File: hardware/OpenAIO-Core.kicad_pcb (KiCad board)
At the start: 6 copper layers, 23 x 20.1 mm, 91 parts, among them J23 SCL, J26 SDA, J30 5V, J34 GND, J35 GND, J37 5V, J38 CAM, J39 VTX, J40 GND, J42 4V5, J43 GND, J44 PIO_TX0, J45 PIO_RX0, J48 RX0, J49 TX0, J50 GND, J52 4V5, J53 GND, J54 TX1, J55 RX1, J91 Core_LGA, Q1 AP1606, Q2 AP1606, U1 TS2306A 240GF MSM 9_C2976675, U10 COS8051SOT, U11 TLV7031DPWR, U2 RP2354A, U6 LP5912-1.8DRVR, U7 LP5912-3.3DRVR, U8 BMI270, U9 SN74LVC1G3157DTBR, X1 XTM25012000JT00351001

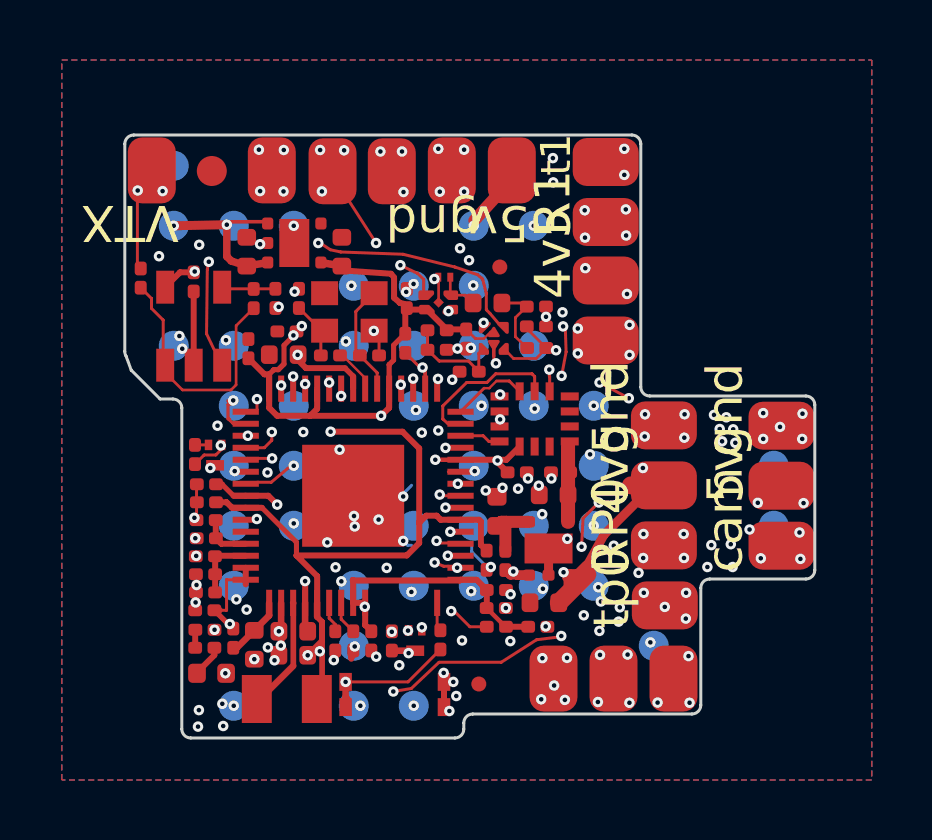
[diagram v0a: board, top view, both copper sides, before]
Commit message: DFM: solder mask 0.04 mm / 0.09 mm web, named X2SON gangs, L3-U25 gap (DFM-12, DFM-11)
Board setup on both boards: solder mask expansion 0 -> 0.04 mm (NextPCB
minimum opening), minimum mask web 0.09 mm (NextPCB green dam; the Core had
none). That made KiCad report 9 Core and 9 Base mask bridges.

Named exceptions, only where the datasheet land pattern has pad gaps below
2 x 0.04 + 0.09 = 0.17 mm: "Mask gang: U9 X2SON-6", "Mask gang: U11
X2SON-4" (Core) and "Mask gang: U23 X2SON-4" (Base), bridged_mask with
severity ignore. KiCad 10.0.6 only matches bridged_mask on item A (an
A && B condition never fires), so each rule names its footprint; no bridge
leaves those footprints.

Real bridges fixed by moving parts (track ends and vias in the pads dragged
along, Base, unconnected 0):
- R65/R66/R64 0201 row +0.02/+0.04/+0.06 mm x (gaps 0.155 -> 0.175)
- R83 -0.015 mm y (R57-R83 gap 0.165 -> 0.18)
- FID1/FID2 (B) 0.04 mm away from U24.11 (web 0.067 -> 0.107)
- U25 -0.015 mm x with its +3V3 via (U25.3-C19.1 0.155 -> 0.17)

DFM-11: U25 (INA186, SC70) and its cap C104 move -0.14 mm y; the L3-U25
body gap goes from 0.075 to 0.215 mm. The CURR track end at U25.6 was set
to (66.00, 52.18) to keep 0.14 mm from the +BATT via at (65.46, 51.83).

With the Core web on, KiCad also reports 5 pad labels clipped by the mask
(single-item). Four of them moved 0.2-0.3 mm (gnd x3, tp0); that also
cleared some old label overlaps. R1 (118.07, 46.86) stays for the owner's
silk pass. The Base '+' label moved 0.1 mm off C104.

DRC (refill, parity) against f193d5f: Core silk_over_copper 12 -> 12, Base
silk_over_copper 27 -> 20, no solder_mask_bridge, every other count
unchanged, unconnected 0 on both boards. DC solve: +BATT 0.582 -> 0.584,
GND 0.358 -> 0.358 mOhm.

Co-Authored-By: Claude Opus 5.5 <noreply@anthropic.com>
Claude-Session: https://claude.ai/code/session_01KTp3FLjVXfXdWrkmr6af7d
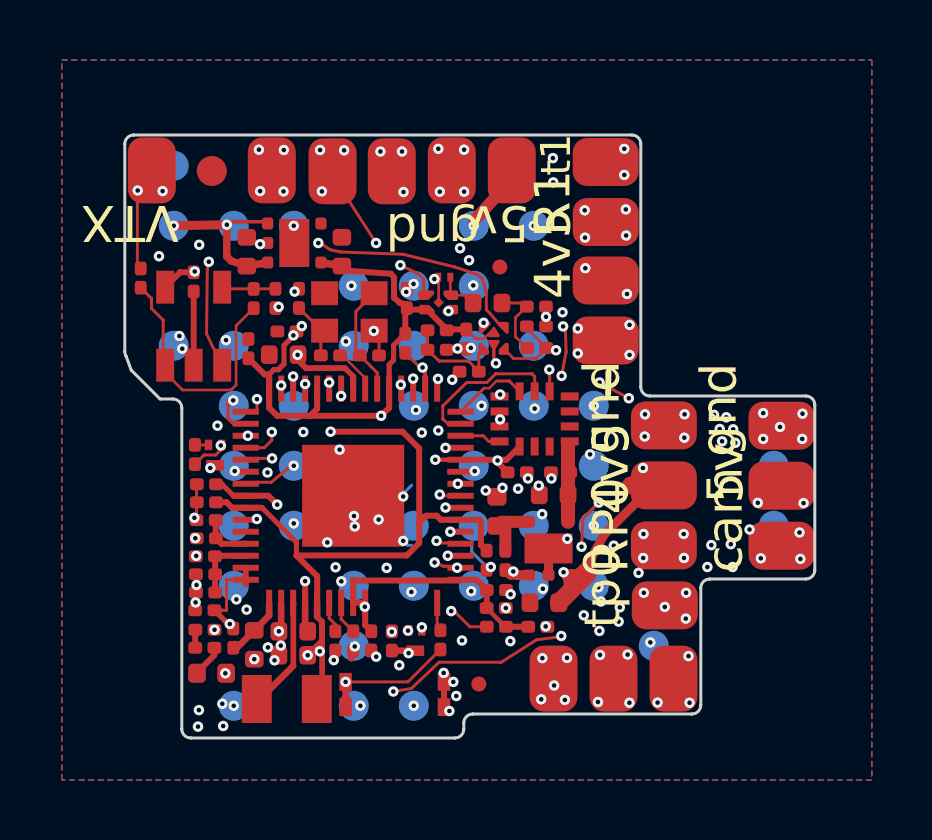
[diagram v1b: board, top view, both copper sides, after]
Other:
- rule pad_to_mask_clearance: 0 -> 0.04

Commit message: DFM: tombstone mitigation on 0201/0402
DFM-07. Metric as in the critique (tomb.py): a 0201/0402 part with a via
in or touching one pad only, and >= 4x more same-net copper within
0.6 mm of one pad centre than the other (zones refilled).

Before -> after (0201 / 0402):
  Core 15 / 4 -> 6 / 1
  Base 33 / 2 -> 26 / 0
If pour beyond a thermal relief counts as attached only through its
spokes: Core 4 / 1, Base 22 / 0.

Thermal relief (per-pad zone connection THERMAL) on the pour-connected
pads of the flagged parts:
- Core: 13 pads. 1 oz outer, so spoke 0.10 and gap 0.15. D1.1, R31.2,
  R26.2 and C6.2 use 45 deg spokes.
- Base: 13 pads. 2 oz outer, so spoke 0.15 and gap 0.20. C82.2 uses
  45 deg spokes.
These pads stay solid because no setting resolved 2 spokes (tried
90/45 deg, smaller gap, spoke 0.20/0.25):
- Core C3.2: 0 spokes. It is the pad's only connection, so it went
  unconnected.
- Base C66.1: 1 spoke.
- Base C66.2 and C43.2: 0 spokes.
No power-path pad is touched. The flagged parts are signal parts,
decoupling caps and LDO caps; +BATT, phase, motor and switch-node pads
were excluded.

Via dog-bones: the via moves just off the pad (ring 0.04-0.25 mm from
the pad), with a neck from the pad centre (Core 0.10, Base 0.15 wide).
Where a track ended in the old via on another layer, a joiner segment
is added.
- Core: R31 (GND), R14 (+5V, In3 joiner), C10 (GND).
- Base: C88 (GND), R39 (MOTOR1, In2 joiner), C67 (2 GND vias).
Clearances were checked on every Cu layer against fixed copper: full
rings, hole clearance, hole-to-hole and edge.

Not changed:
- Vias shared with another part's pad were not moved: R26/C31,
  C73/JP1, R38/C18/Card1, C65/U12, C66/U12.
- 19 Base gate and divider resistors are still flagged. Both ends have
  under 0.2 mm2 of copper; the ratio is a 0.06-0.08 mm2 track against
  the in-pad via. There is no room: a moved through via hits F.Cu or
  In2 copper within 0.5 mm.
- No matching via was added. The other ends have no same-net inner
  copper, so su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
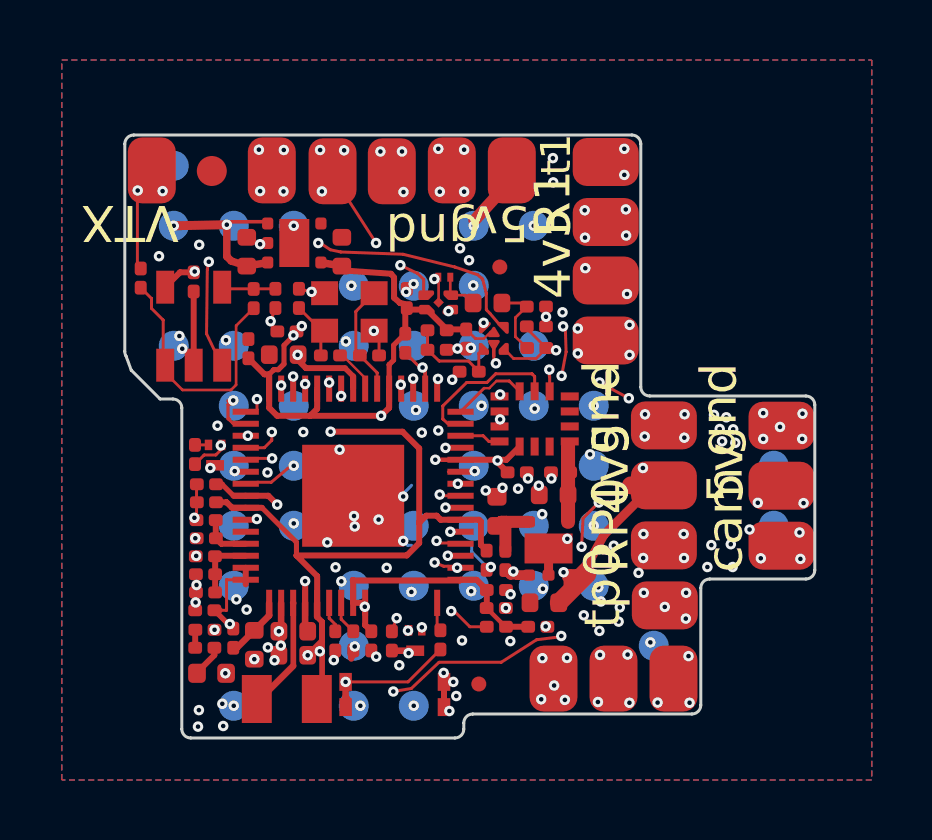
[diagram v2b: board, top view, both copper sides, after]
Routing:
- net +5V: track 37.4 -> 38.5 mm
- net GND: track 16.0 -> 16.9 mm
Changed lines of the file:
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@@
 			(pinfunction "K_1")
 			(pintype "passive")
+			(zone_connect 1)
+			(thermal_bridge_width 0.1)
+			(thermal_bridge_angle 45)
+			(thermal_gap 0.15)
 		)
 		(pad "2" smd roundrect
@@
 			(net "GND")
 			(pintype "passive")
+			(zone_connect 1)
+			(thermal_bridge_width 0.1)
+			(thermal_gap 0.15)
 		)
 		(embedded_fonts no)
@@
 			(net "GND")
 			(pintype "passive")
+			(zone_connect 1)
+			(thermal_bridge_width 0.1)
+			(thermal_gap 0.15)
 		)
 		(embedded_fonts no)
@@
 			(net "GND")
 			(pintype "passive")
+			(zone_connect 1)
+			(thermal_bridge_width 0.1)
+			(thermal_bridge_angle 45)
+			(thermal_gap 0.15)
 		)
 		(embedded_fonts no)
@@
 			(net "GND")
 			(pintype "passive")
+			(zone_connect 1)
+			(thermal_bridge_width 0.1)
+			(thermal_bridge_angle 45)
+			(thermal_gap 0.15)
 		)
 		(embedded_fonts no)
@@
 			(net "GND")
 			(pintype "passive")
+			(zone_connect 1)
+			(thermal_bridge_width 0.1)
+			(thermal_bridge_angle 45)
+			(thermal_gap 0.15)
 		)
 		(embedded_fonts no)
@@
 			(net "GND")
 			(pintype "passive")
+			(zone_connect 1)
+			(thermal_bridge_width 0.1)
+			(thermal_gap 0.15)
 		)
 		(embedded_fonts no)
@@
 			(net "GND")
 			(pintype "passive")
+			(zone_connect 1)
+			(thermal_bridge_width 0.1)
+			(thermal_gap 0.15)
 		)
 		(pad "2" smd roundrect
@@
 			(net "GND")
 			(pintype "passive")
+			(zone_connect 1)
+			(thermal_bridge_width 0.1)
+			(thermal_gap 0.15)
 		)
 		(embedded_fonts no)
@@
 			(net "GND")
 			(pintype "passive")
+			(zone_connect 1)
+			(thermal_bridge_width 0.1)
+			(thermal_gap 0.15)
 		)
 		(embedded_fonts no)
@@
 			(net "GND")
 			(pintype "passive")
+			(zone_connect 1)
+			(thermal_bridge_width 0.1)
+			(thermal_gap 0.15)
 		)
 		(pad "2" smd roundrect
@@
 			(net "GND")
 			(pintype "passive")
+			(zone_connect 1)
+			(thermal_bridge_width 0.1)
+			(thermal_gap 0.15)
 		)
 		(embedded_fonts no)
@@
 			(net "GND")
 			(pintype "passive")
+			(zone_connect 1)
+			(thermal_bridge_width 0.1)
+			(thermal_gap 0.15)
 		)
 		(pad "2" smd roundrect
@@
 	)
 	(segment
+		(start 108.1212 49.2675)
+		(end 107.9612 49.7075)
+		(width 0.1)
+		(layer "F.Cu")
+		(net "GND")
+	)
+	(segment
 		(start 115.4 51.04)
 		(end 115.4 50.866448)
@@
 	)
 	(segment
+		(start 108.905 48.6275)
+		(end 109.325 48.7275)
+		(width 0.1)
+		(layer "F.Cu")
+		(net "GND")
+	)
+	(segment
 		(start 114.55 50.57)
 		(end 114.46 50.66)
@@
 	)
 	(via
-		(at 108.76 48.72)
+		(at 109.325 48.7275)
 		(size 0.35)
 		(drill 0.15)
@@
 	)
 	(via
-		(at 108.23 49.23)
+		(at 107.9612 49.7075)
 		(size 0.35)
 		(drill 0.15)
@@
 	)
 	(segment
+		(start 112.0025 60.045)
+		(end 112.1625 59.605)
+		(width 0.1)
+		(layer "F.Cu")
+		(net "+5V")
+	)
+	(segment
 		(start 112.0025 60.0575)
 		(end 112 60.06)
@@
 	)
 	(via
-		(at 112 60.06)
+		(at 112.1625 59.605)
 		(size 0.35)
 		(drill 0.15)
@@
 		(net "+5V")
 	)
+	(segment
+		(start 112.05 60.15)
+		(end 112.1625 59.605)
+		(width 0.1)
+		(layer "In3.Cu")
+		(net "+5V")
+	)

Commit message: Silk: pad function labels on both boards (FB5 item 1, V1/V2/V4/M5)
Old board-level labels removed and re-placed by script (pcbnew API):
KiCad stroke font 0.8/0.6/0.13 mm (0.65/0.5/0.1 where 0.8 does not fit),
codes of at most 3 characters, each label nearer its own pad than any
other labelled pad, 0.19 mm from mask openings, 0.25 mm from the edge,
off component bodies and off the Core footprint on the Base.

- Core: 17 of 20 pads labelled (VTX, GND, SDA, 5V, RX1, 4V5, RX0, TX0,
  PTX, CAM ...). No room for J23 SCL, J54 TX1, J48 PRX: README legend.
  UART codes follow config.h (J44/J45 = UART0 TX0/RX0, J49/J48 =
  PIOUART0 PTX/PRX).
- Base: corner 5V/LED/GND pads (GND on B), battery + and - at equal
  size, BZ+/BZ- (was B+/B-), ESC SWD test pads SDn/SCn, BT0. No room for
  J41/J51 (10V/GND), TP31/TP32 (SWD/SWC), TP2, TP5, TP7: README legend.
- Motor pads: no room within 3.5 mm on either side, so B.Silk carries a
  motor map (M1-M4 at the positions of their pad groups).
- Old B.Silk 'Open' text and 'AIO' polygons (on 61 vias) removed to free
  the room; identity follows in item 3.

Copper unchanged (geometry hash). DRC errors: Base 45 -> 39
(silk_over_copper 20 -> 15, silk_edge 4 -> 3), Core 42 -> 28 (silk 14 ->
0); unconnected 0/0; parity unchanged. The Tokyo font is not installed
here, so the saved render caches of the remaining Tokyo text ('DJI') are
substitutes.

Co-Authored-By: Claude Opus 5.5 <noreply@anthropic.com>
Claude-Session: https://claude.ai/code/session_01KTp3FLjVXfXdWrkmr6af7d
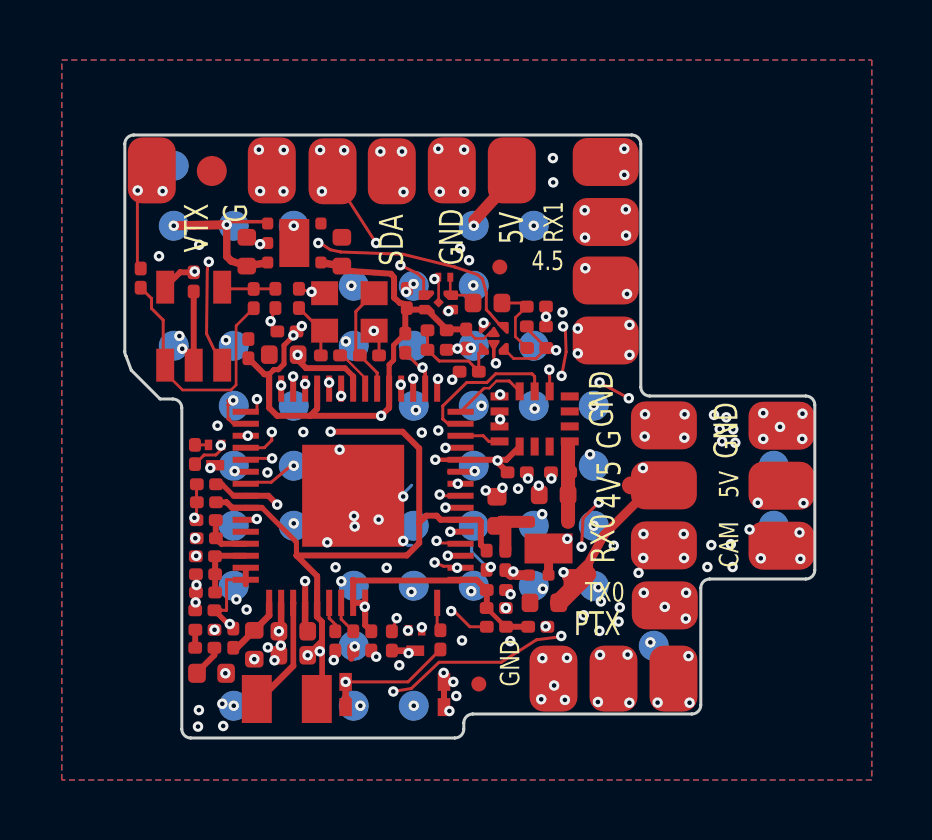
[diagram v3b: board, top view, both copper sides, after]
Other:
- board text added: "4.5"
- board text added: "4V5"
- board text added: "5V"
- board text added: "CAM"
- board text added: "G"
- board text added: "GND"
- board text added: "PTX"
- board text added: "RX0"
- board text added: "RX1"
- board text added: "SDA"
- board text added: "TX0"
- board text removed: "4v5"
- board text removed: "5v"
- board text removed: "R1"
- board text removed: "RP0"
- board text removed: "cam"
- board text removed: "gnd"
- board text removed: "t1"
- board text removed: "tp0"
